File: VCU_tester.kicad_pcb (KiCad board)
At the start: 2 copper layers, 200 x 159 mm, 121 parts, among them J1 Conn_01x04_Male, J10 DB9_Male, J11 DB9_Male, J12 Conn_01x08_Male, J13 Conn_01x08_Male, J14 USB_C_Receptacle, J15 USB_B_Micro, J2 Screw_Terminal_01x02, J3 DB9_Male, J4 DB9_Male, J5 DB9_Male, J500 Conn_01x10_Female, J501 Conn_01x08_Female, J502 Conn_01x08_Female, J503 Conn_01x08_Female, J504 Conn_01x08_Female, J505 Conn_01x08_Female, J507 Conn_02x18_Odd_Even, J6 DB9_Male, J7 Conn_01x04_Male, J8 DB9_Male, J9 DB9_Male, P8 BeagleBone_Black_Header, P9 BeagleBone_Black_Header, U1 REF3020, U2 MAX3232, U3 TCAN1042HVD, U4 MAX3232, U5 TCAN1042HVD, U6 DS3231MZ, U7 DS3231MZ

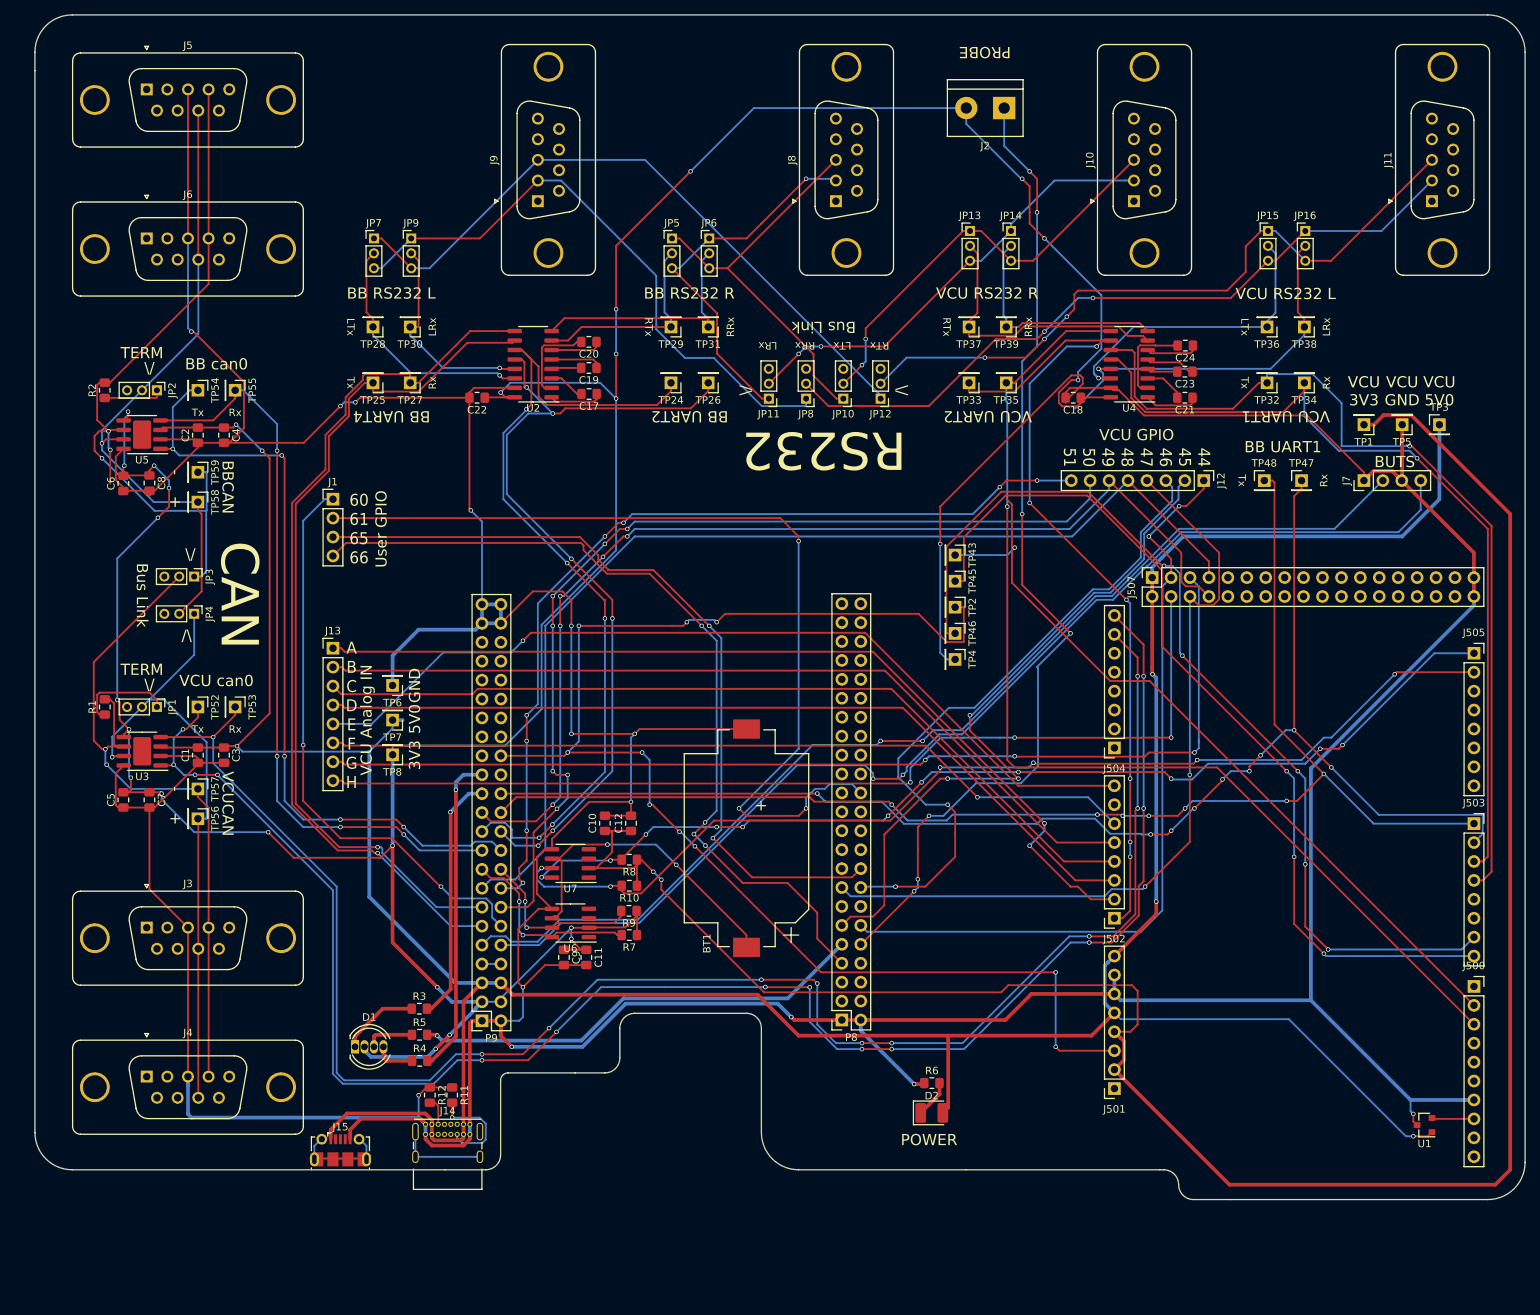
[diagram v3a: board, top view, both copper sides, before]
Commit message: better routing, tcan footprint, mount holes + silkscreen
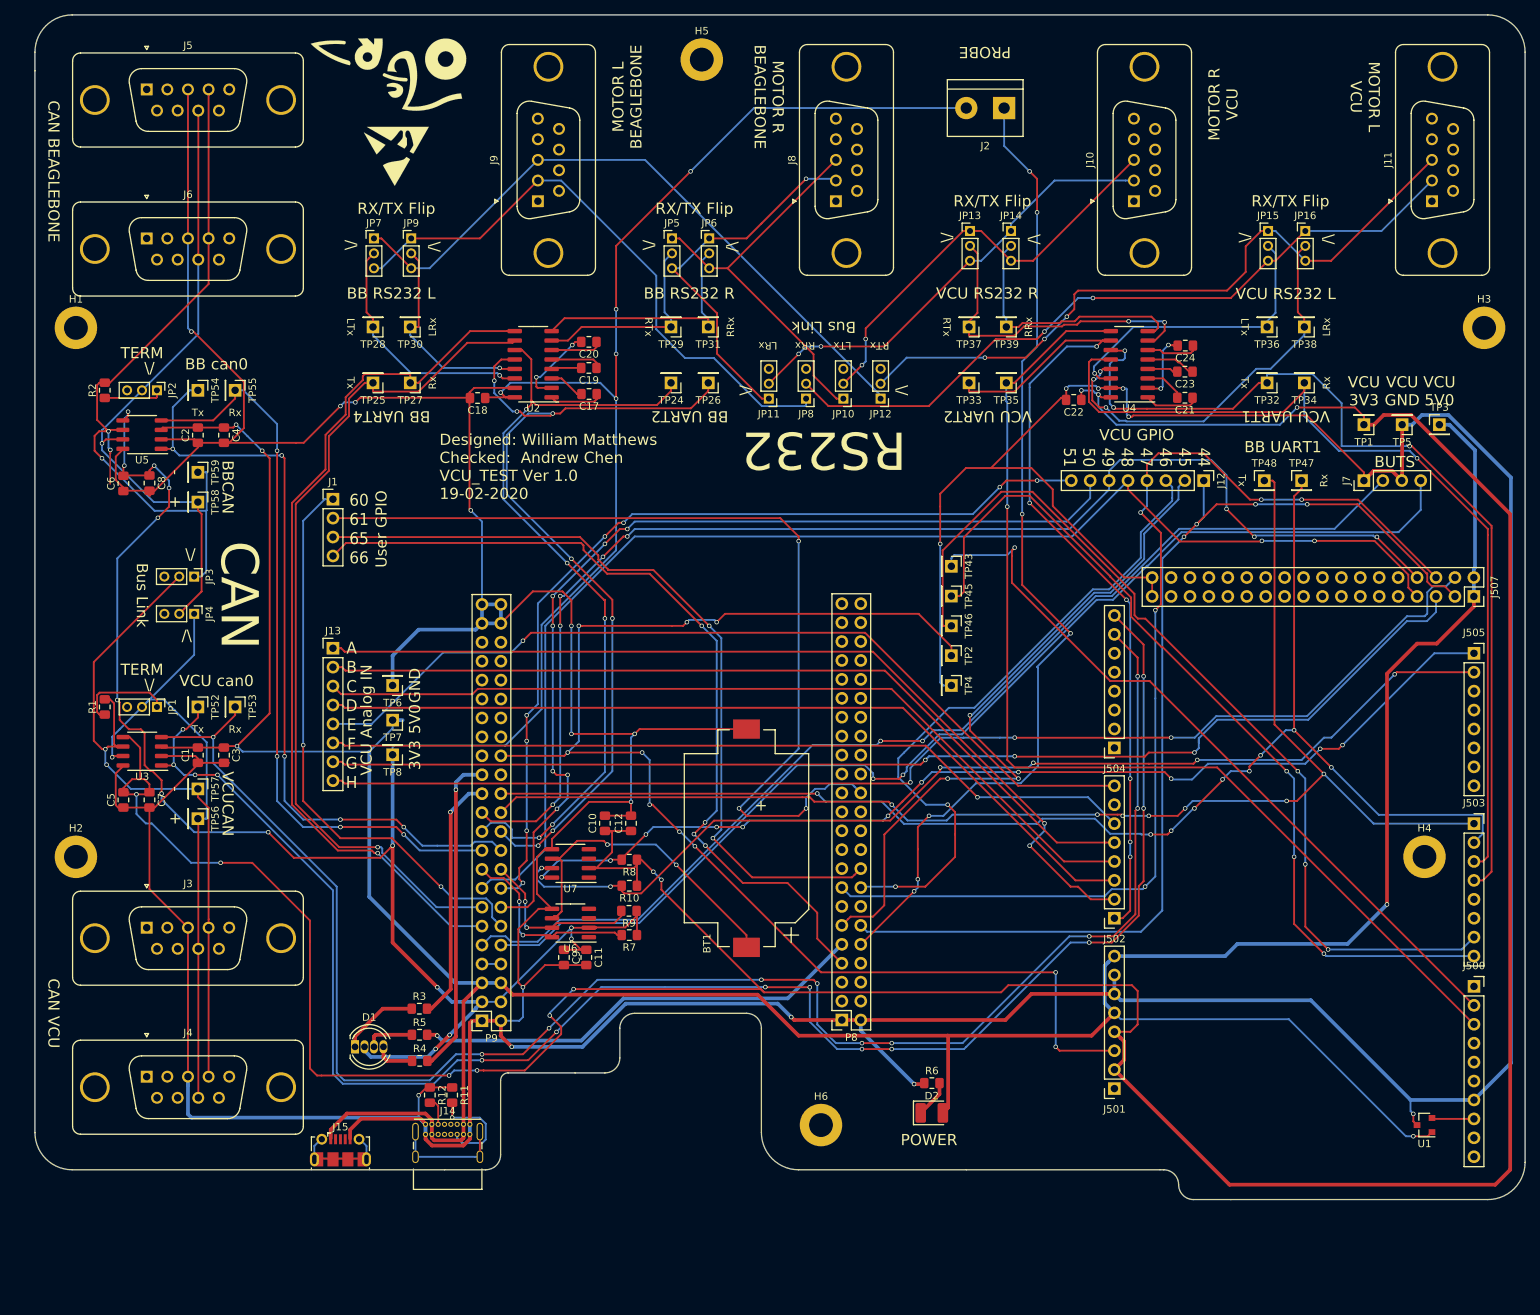
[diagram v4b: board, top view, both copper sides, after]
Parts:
- added G***: LOGO, footprints:OUR-Logo, F.Cu at (45.0, -17.0)
- added H1: MountingHole, MountingHole:MountingHole_3.2mm_M3_ISO7380_Pad, F.Cu at (3.00, 17.0)
- added H2: MountingHole, MountingHole:MountingHole_3.2mm_M3_ISO7380_Pad, F.Cu at (3.00, 88.0)
- added H3: MountingHole, MountingHole:MountingHole_3.2mm_M3_ISO7380_Pad, F.Cu at (192.0, 17.0)
- added H4: MountingHole, MountingHole:MountingHole_3.2mm_M3_ISO7380_Pad, F.Cu at (184.0, 88.0)
- added H5: MountingHole, MountingHole:MountingHole_3.2mm_M3_ISO7380_Pad, F.Cu at (87.0, -19.0)
- added H6: MountingHole, MountingHole:MountingHole_3.2mm_M3_ISO7380_Pad, F.Cu at (103.0, 124.0)
- added REF**: ESD-Logo_8.9x8mm_SilkScreen, Symbol:ESD-Logo_8.9x8mm_SilkScreen, F.Cu at (46.0, -6.00)
- U3, U5: footprint Package_SO:SOIC-8-1EP_3.9x4.9mm_P1.27mm_EP2.41x3.81mm -> Package_SO:SO-8_3.9x4.9mm_P1.27mm
- moved C22 80.1 mm to (136.9, 26.7)
- moved C18 79.9 mm to (56.9, 26.4)
- moved J507 43.2 mm to (190.6, 53.0), turned to 270 degrees
- moved TP2 6.52 mm to (120.5, 61.0)
- moved TP4 3.54 mm to (120.5, 65.0)
- moved TP45 2.06 mm to (120.5, 53.0)
- moved TP43 1.58 mm to (120.5, 49.0)
- moved TP46 1.12 mm to (120.5, 57.0)
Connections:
- C22 pad 1: +3V3 -> +3.3VA
- C5 pad 2: +3V3 -> +3.3VA
- C7 pad 1: +3V3 -> +3.3VA
- U3 pad 5: +3V3 -> +3.3VA
- U4 pad 16: +3V3 -> +3.3VA
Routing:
- net +3.3VA: track 286.6 -> 472.2 mm, vias 2 -> 11
- net +3V3: track 429.4 -> 367.1 mm, vias 24 -> 19
- net GNDD: track 817.0 -> 869.1 mm, vias 15 -> 19
- net /GPIO_47: track 107.8 -> 147.1 mm, vias 2 -> 5
- net /GPIO_44: track 105.0 -> 143.5 mm, vias 2 -> 4
- net /GPIO_49: track 142.3 -> 172.7 mm, vias 5 -> 8
- net /PressLout: track 135.2 -> 165.0 mm
- net /GPIO_48: track 144.5 -> 174.0 mm, vias 0 -> 2
- net /PressLin: track 141.1 -> 160.0 mm
- net /VCURXD1A: track 114.6 -> 121.6 mm
- net /UART2_TXD: track 114.8 -> 108.4 mm
- net /GPIO_4: track 106.7 -> 100.6 mm
- net +5V: track 441.9 -> 447.9 mm, vias 6 -> 5
- net /GPIO_112: track 186.0 -> 180.0 mm
- net /UART2_RXD: track 111.6 -> 117.4 mm, vias 6 -> 7
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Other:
- board text added: "CAN BEAGLEBONE"
- board text added: "CAN VCU"
- board text added: "Designed: William Matthews Checked: Andrew Chen VCU_TEST Ver 1.0 19-02-2020"
- board text added: "MOTOR L BEAGLEBONE"
- board text added: "MOTOR L VCU"
- board text added: "MOTOR R BEAGLEBONE"
- board text added: "MOTOR R VCU"
- board text added: "RX/TX Flip"
- board text added: "Stacked DSUB: 178-009-613R491"
- board text removed: "178-009-613R491"

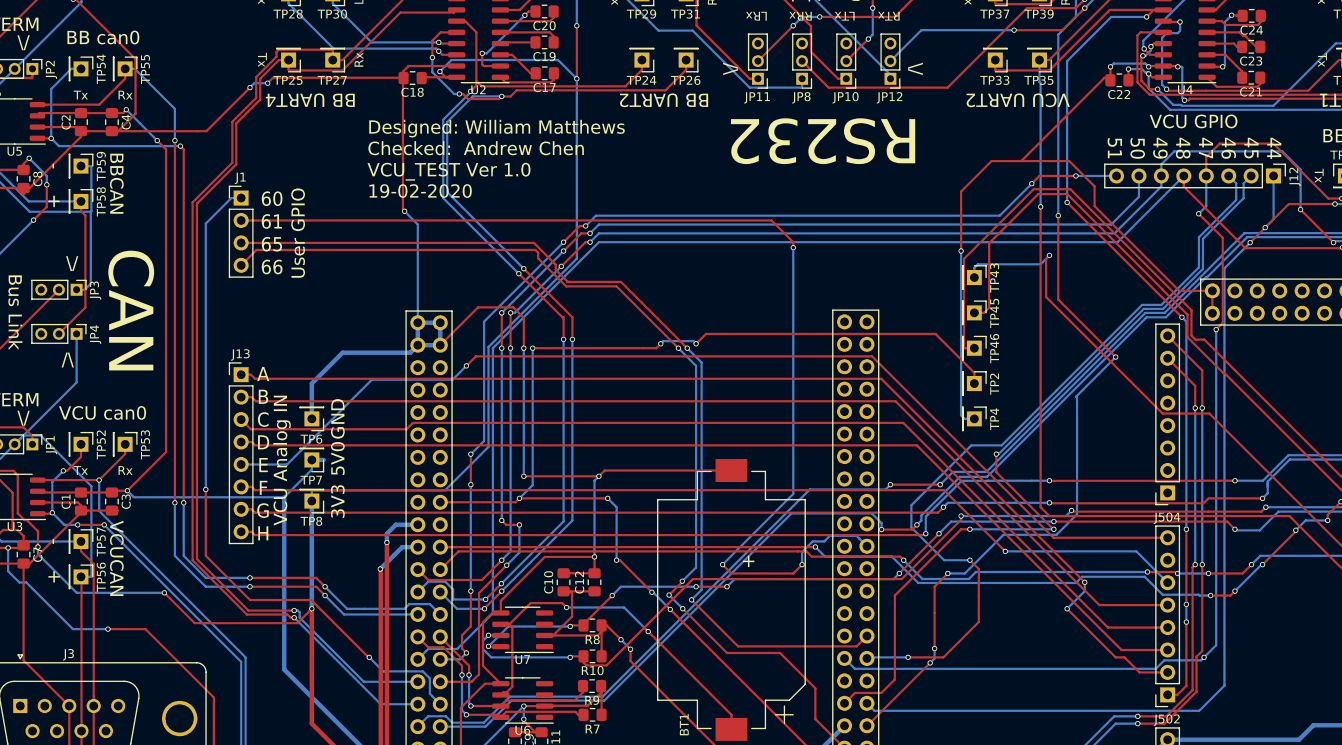
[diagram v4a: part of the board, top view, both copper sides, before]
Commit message: reassigned brake, emsdc, audio vcurst, better testpoint
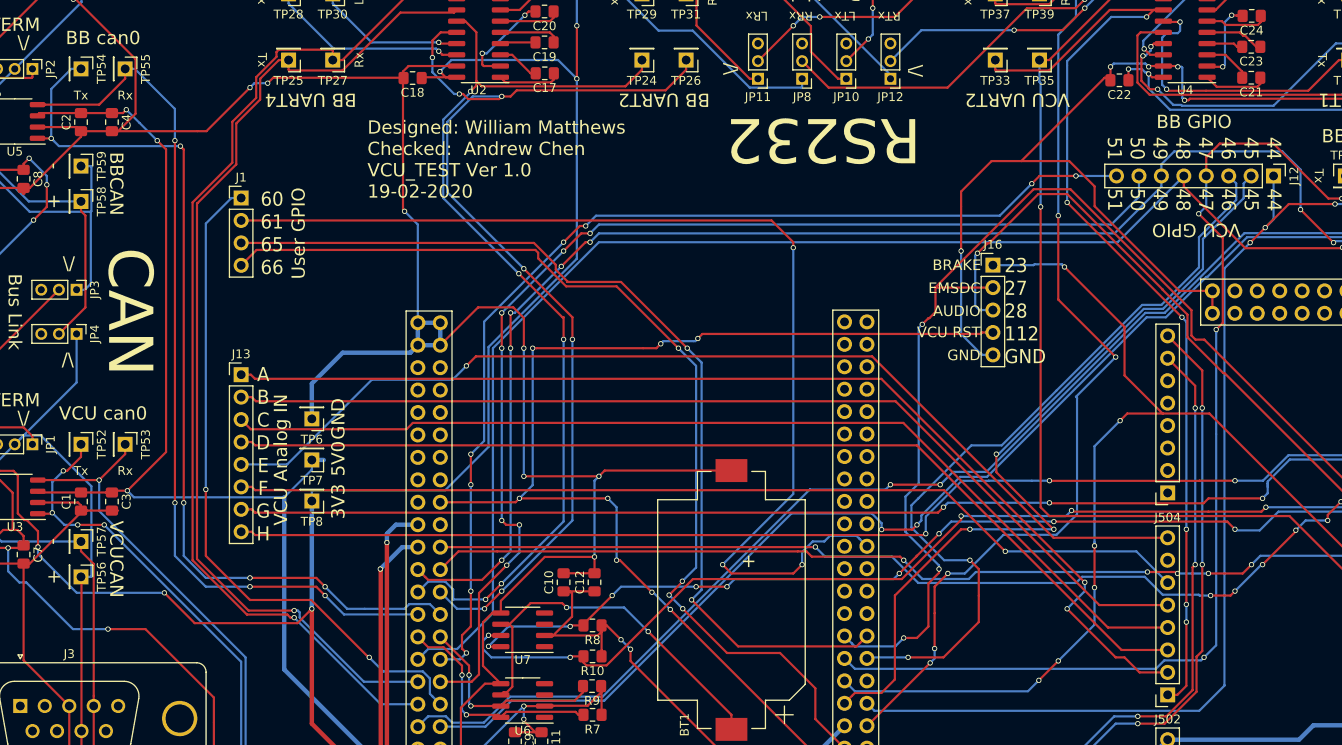
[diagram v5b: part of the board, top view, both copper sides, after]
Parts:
- removed TP2, TP4, TP43, TP45, TP46: TestPoint, Connector_PinHeader_2.54mm:PinHeader_1x01_P2.54mm_Vertical
- added J16: Conn_01x05_Male, Connector_PinHeader_2.54mm:PinHeader_1x05_P2.54mm_Vertical, F.Cu at (122.6, 47.6)
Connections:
- J500 pad 2: /GPIO_4 -> /GPIO_23
- J503 pad 7: /GPIO_7 -> /GPIO_27
- J503 pad 8: /GPIO_5 -> /GPIO_28
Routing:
- net /GPIO_27: track 0.00 -> 178.0 mm, vias 0 -> 6
- net /GPIO_23: track 0.00 -> 157.7 mm, vias 0 -> 6
- net /GPIO_7: track 125.3 -> 0.00 mm, vias 3 -> 0
- net /GPIO_28: track 0.00 -> 119.3 mm, vias 0 -> 4
- net /GPIO_5: track 118.5 -> 0.00 mm, vias 3 -> 0
- net /GPIO_4: track 100.6 -> 0.00 mm, vias 1 -> 0
- net GNDD: track 869.1 -> 862.8 mm
- net /GPIO_112: track 180.0 -> 178.9 mm
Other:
- board text added: "23 27 28 112 GND"
- board text added: "AUDIO"
- board text added: "BB GPIO"
- board text added: "BRAKE"
- board text added: "EMSDC"
- board text added: "VCU RST"

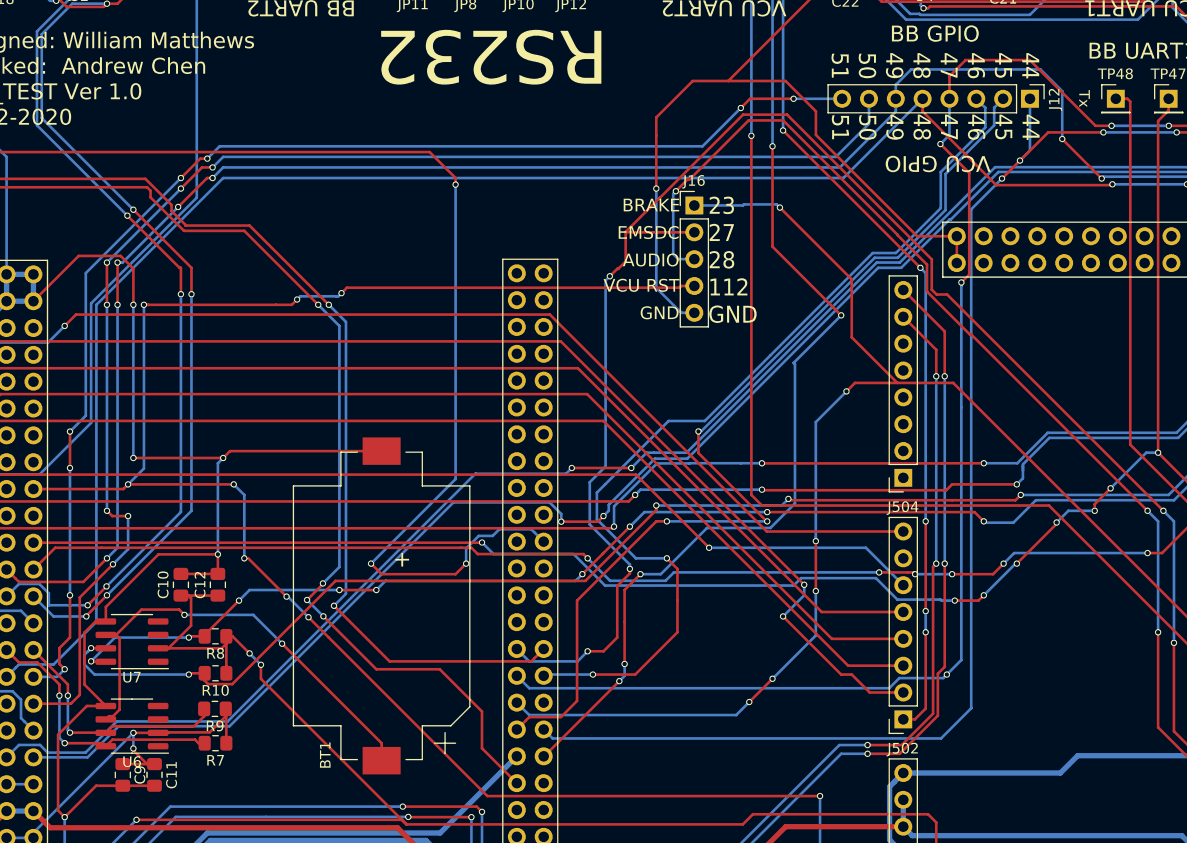
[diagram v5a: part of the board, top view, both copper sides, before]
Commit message: add decouple caps, add gpios
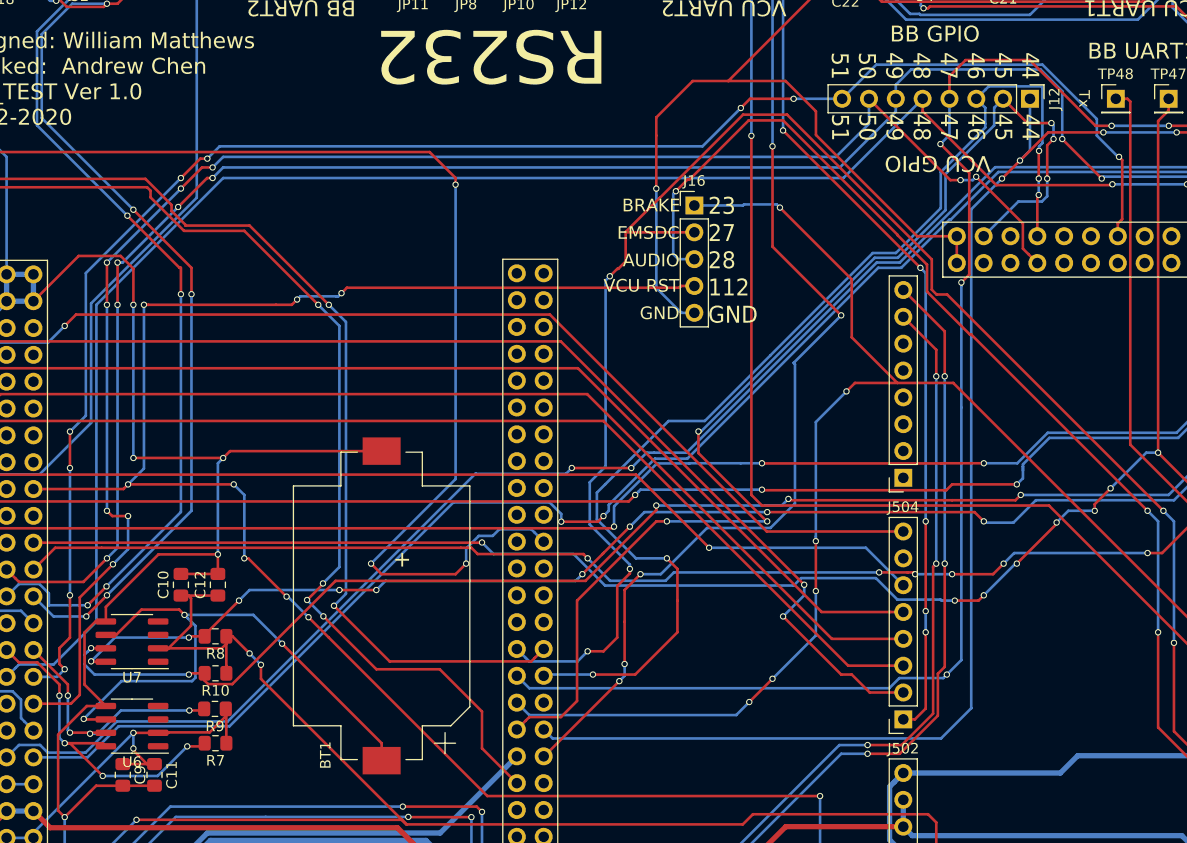
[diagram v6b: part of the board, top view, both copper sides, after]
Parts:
- C10, C9: value 100p -> 100n
- C11, C12: value 10n -> 1u
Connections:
- J507 pad 24: Net-(J507-Pad24) -> /GPIO_51
- J507 pad 29: Net-(J507-Pad29) -> /GPIO_50
- J507 pad 30: Net-(J507-Pad30) -> /GPIO_46
- J507 pad 34: Net-(J507-Pad34) -> /GPIO_45
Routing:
- net /GPIO_51: track 120.4 -> 160.3 mm, vias 8 -> 9
- net /GPIO_50: track 129.2 -> 153.2 mm, vias 7 -> 9
- net /GPIO_46: track 88.6 -> 109.7 mm, vias 2 -> 5
- net /GPIO_45: track 93.5 -> 113.9 mm, vias 3 -> 6
- net /RTC_VBAT: track 42.9 -> 54.7 mm, vias 2 -> 3
- net /I2C1_SCL: track 25.9 -> 31.9 mm, vias 2 -> 4
- net /I2C1_SDA: track 23.3 -> 24.6 mm, vias 2 -> 4
